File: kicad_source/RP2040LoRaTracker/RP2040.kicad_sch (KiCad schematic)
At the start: 29 parts, among them J1 USB_B_Micro, SW1 SW_Push, SW2 SW_Push, U1 RP2040, U4 W25Q16JVSS, Y1 Crystal_GND24_Small

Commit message: started layout
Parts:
- J1: footprint (none) -> Connector_USB:USB_Micro-B_Molex_47346-0001
- SW1, SW2: footprint (none) -> Button_Switch_SMD:SW_Tactile_SPST_NO_Straight_CK_PTS636Sx25SMTRLFS
- Y1: footprint (none) -> Crystal:Crystal_SMD_3225-4Pin_3.2x2.5mm
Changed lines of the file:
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@@
 			)
 		)
-		(property "Footprint" ""
+		(property "Footprint" "Button_Switch_SMD:SW_Tactile_SPST_NO_Straight_CK_PTS636Sx25SMTRLFS"
 			(at 45.72 50.8 0)
 			(effects
@@
 			)
 		)
-		(property "Footprint" ""
+		(property "Footprint" "Connector_USB:USB_Micro-B_Molex_47346-0001"
 			(at 34.29 152.4 0)
 			(effects
@@
 			)
 		)
-		(property "Footprint" ""
+		(property "Footprint" "Crystal:Crystal_SMD_3225-4Pin_3.2x2.5mm"
 			(at 77.47 116.84 0)
 			(effects
@@
 			)
 		)
-		(property "Footprint" ""
+		(property "Footprint" "Button_Switch_SMD:SW_Tactile_SPST_NO_Straight_CK_PTS636Sx25SMTRLFS"
 			(at 45.72 38.1 0)
 			(effects

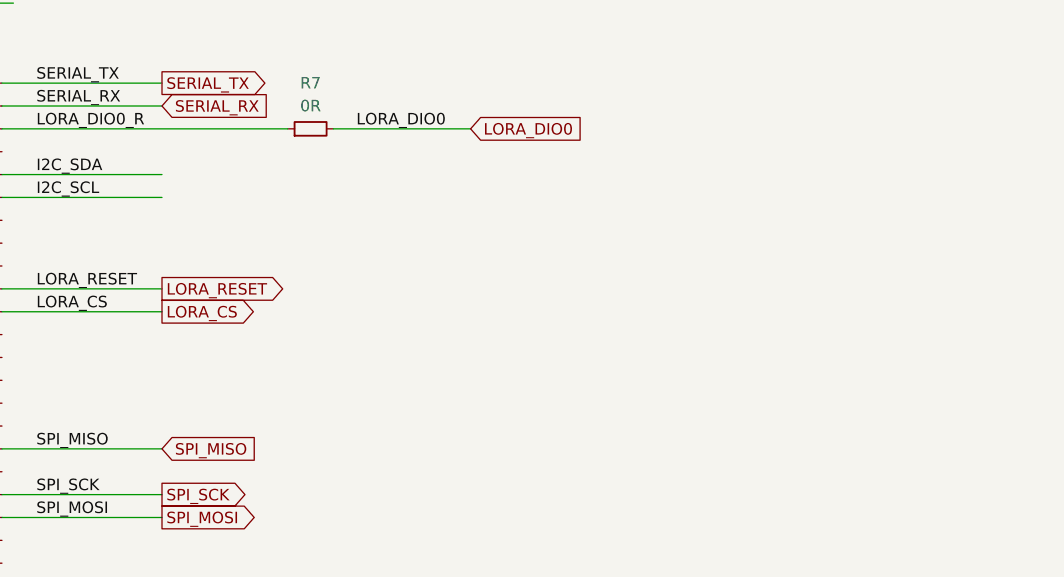
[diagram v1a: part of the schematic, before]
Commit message: added BME280 and quiic connector
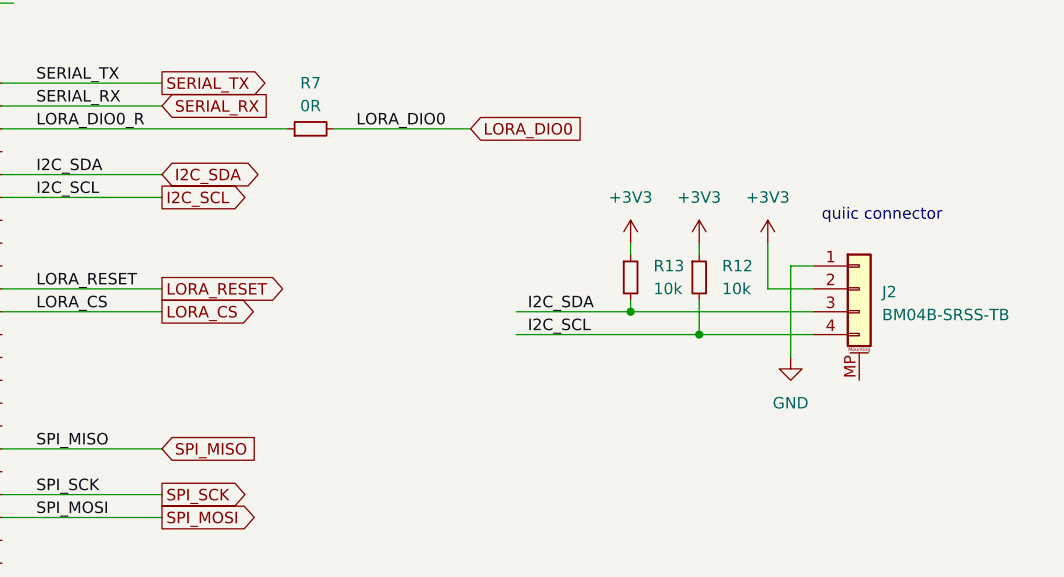
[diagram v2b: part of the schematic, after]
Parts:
- added J2: BM04B-SRSS-TB, Connector_JST:JST_SH_BM04B-SRSS-TB_1x04-1MP_P1.00mm_Vertical, symbol Connector_Generic_MountingPin:Conn_01x04_MountingPin
- added R12, R13: 10k, Resistor_SMD:R_0603_1608Metric, symbol Device:R_Small
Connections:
- net +3V3: now also J2.2 (Pin_2), R12.1, R13.1
- net GND: now also J2.1 (Pin_1)
- net I2C_SCL: now also J2.4 (Pin_4), R12.2
- net I2C_SDA: now also J2.3 (Pin_3), R13.2
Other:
- note added: "quiic connector"

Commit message: added battery charger
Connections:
- net VBUS: now reaches J1.1 (VBUS)
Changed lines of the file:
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@@
 	(wire
 		(pts
+			(xy 38.1 146.05) (xy 43.18 146.05)
+		)
+		(stroke
+			(width 0)
+			(type default)
+		)
+	)
+	(wire
+		(pts
 			(xy 146.05 53.34) (xy 146.05 46.99)
 		)
@@
 	(wire
 		(pts
+			(xy 43.18 146.05) (xy 43.18 142.24)
+		)
+		(stroke
+			(width 0)
+			(type default)
+		)
+	)
+	(wire
+		(pts
 			(xy 238.76 78.74) (xy 238.76 80.01)
 		)
@@
 					(unit 1)
 				)
+			)
+		)
+	)
+	(symbol
+		(lib_id "power:VBUS")
+		(at 43.18 142.24 0)
+		(unit 1)
+		(exclude_from_sim no)
+		(in_bom yes)
+		(on_board yes)
+		(dnp no)
+		(fields_autoplaced yes)
+		(property "Reference" "#PWR94"
+			(at 43.18 146.05 0)
+			(effects
+				(font
+					(size 1.27 1.27)
+				)
+				(hide yes)
+			)
+		)
+		(property "Value" "VBUS"
+			(at 43.18 137.16 0)
+			(effects
+				(font
+					(size 1.27 1.27)
+				)
+			)
+		)
+		(property "Footprint" ""
+			(at 43.18 142.24 0)
+			(effects
+				(font
+					(size 1.27 1.27)
+				)
+				(hide yes)
+			)
+		)
+		(property "Datasheet" ""
+			(at 43.18 142.24 0)
+			(effects
+				(font
+					(size 1.27 1.27)
+				)
+				(hide yes)
+			)
+		)
+		(property "Description" "Power symbol creates a global label with name \"VBUS\""
+			(at 43.18 142.24 0)
+			(effects
+				(font
+					(size 1.27 1.27)
+				)
+				(hide yes)
+			)
+		)
+		(pin "1"
+		)
+		(instances
+			(project "RP2040LoRaTracker"
+				(path "/143f7a5b-9016-4d2c-b741-f535648590f8/910e63e5-4a03-4b20-a38f-348d4b59ea4e"
+					(reference "#PWR94")
+					(unit 1)
+				)

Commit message: updated some values in schematic, added comments, updated schematic pdf
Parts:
- R7: value 0R -> DNI
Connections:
- no-connect marks 1 -> 22
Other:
- note added: "0R"
- note added: "BOOT"
- note added: "RESET"
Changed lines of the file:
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@@
 	(title_block
 		(title "RP2040LoRaTracker")
-		(date "2025-04-01")
+		(date "2025-04-20")
 		(rev "0.1")
 		(company "generationmake")
@@
 	)
 	(no_connect
+		(at 161.29 76.2)
+	)
+	(no_connect
+		(at 161.29 96.52)
+	)
+	(no_connect
+		(at 161.29 137.16)
+	)
+	(no_connect
+		(at 161.29 121.92)
+	)
+	(no_connect
+		(at 161.29 93.98)
+	)
+	(no_connect
 		(at 38.1 156.21)
 	)
+	(no_connect
+		(at 110.49 127)
+	)
+	(no_connect
+		(at 161.29 129.54)
+	)
+	(no_connect
+		(at 161.29 132.08)
+	)
+	(no_connect
+		(at 161.29 114.3)
+	)
+	(no_connect
+		(at 110.49 129.54)
+	)
+	(no_connect
+		(at 161.29 68.58)
+	)
+	(no_connect
+		(at 161.29 104.14)
+	)
+	(no_connect
+		(at 161.29 81.28)
+	)
+	(no_connect
+		(at 161.29 91.44)
+	)
+	(no_connect
+		(at 161.29 134.62)
+	)
+	(no_connect
+		(at 161.29 116.84)
+	)
+	(no_connect
+		(at 161.29 119.38)
+	)
+	(no_connect
+		(at 161.29 78.74)
+	)
+	(no_connect
+		(at 161.29 111.76)
+	)
+	(no_connect
+		(at 161.29 99.06)
+	)
+	(no_connect
+		(at 161.29 88.9)
+	)
 	(wire
 		(pts
@@
 		)
 	)
+	(text "BOOT"
+		(exclude_from_sim no)
+		(at 54.356 52.832 0)
+		(effects
+			(font
+				(size 1.27 1.27)
+			)
+		)
+	)
+	(text "0R"
+		(exclude_from_sim no)
+		(at 195.58 69.088 0)
+		(effects
+			(font
+				(size 1.27 1.27)
+			)
+		)
+	)
+	(text "RESET"
+		(exclude_from_sim no)
+		(at 54.61 40.894 0)
+		(effects
+			(font
+				(size 1.27 1.27)
+			)
+		)
+	)
 	(label "LORA_CS"
 		(at 165.1 86.36 0)
@@
 			)
 		)
-		(property "Value" "0R"
+		(property "Value" "DNI"
 			(at 195.58 63.5 90)
 			(effects

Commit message: set charging current to 500 mA (R15=2k)
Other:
- note added: "or IS25LP016D"
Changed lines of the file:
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@@
 	(title_block
 		(title "RP2040LoRaTracker")
-		(date "2025-04-20")
+		(date "2025-05-04")
 		(rev "0.1")
 		(company "generationmake")
@@
 		(effects
 			(font
+				(size 1.27 1.27)
+			)
+		)
+	)
+	(text "or IS25LP016D"
+		(exclude_from_sim no)
+		(at 32.258 90.932 0)
+		(effects
+			(font

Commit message: fixed all 3d models in footprints
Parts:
- U4: footprint Package_SO:SOIC-8_5.23x5.23mm_P1.27mm -> Package_SO:SOIC-8_5.275x5.275mm_P1.27mm
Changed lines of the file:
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@@
 			)
 		)
-		(property "Footprint" "Package_SO:SOIC-8_5.23x5.23mm_P1.27mm"
+		(property "Footprint" "Package_SO:SOIC-8_5.275x5.275mm_P1.27mm"
 			(at 49.53 86.36 0)
 			(effects

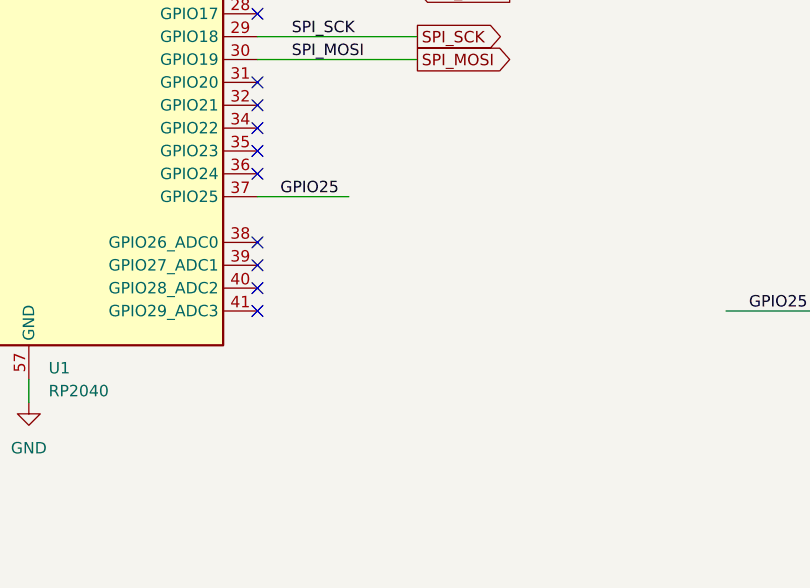
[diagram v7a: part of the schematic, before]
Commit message: added battery voltage measurement, R17 and R18
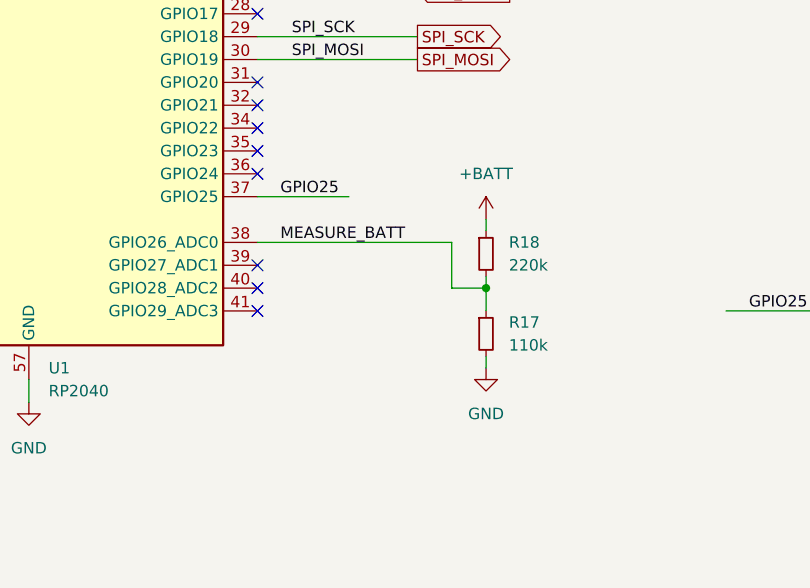
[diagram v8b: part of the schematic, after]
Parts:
- added R17: 110k, Resistor_SMD:R_0603_1608Metric, symbol Device:R_Small
- added R18: 220k, Resistor_SMD:R_0603_1608Metric, symbol Device:R_Small
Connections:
- net GND: now also R17.2
- net MEASURE_BATT: now reaches U1.38 (GPIO26_ADC0)
- net MEASURE_BATT: now also R17.1, R18.2
- new net +BATT: R18.1
- no-connect marks 22 -> 21
